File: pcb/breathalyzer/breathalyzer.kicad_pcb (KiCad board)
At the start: 2 copper layers, 18 parts, among them IC1 TPS3840DL25DBVR, J1 10129379-906002BLF, U1 STM32F030K6Tx, U2 TLV73325PDBV, U3 TLV61070ADBV

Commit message: reset button
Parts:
- added SW1: PTS636SK43SMTR, breathalyzer:PTS636SM43JSMTRLFS, F.Cu at (154.2, 119.4)
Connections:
- J1 pad 5: unconnected-(J1-Pad5) -> SWCLK
- J1 pad 6: unconnected-(J1-Pad6) -> SWDIO
- U1 pad 23: unconnected-(U1-PA13-Pad23) -> SWDIO
- U1 pad 24: unconnected-(U1-PA14-Pad24) -> SWCLK
- U1 pad 4: unconnected-(U1-NRST-Pad4) -> NRST

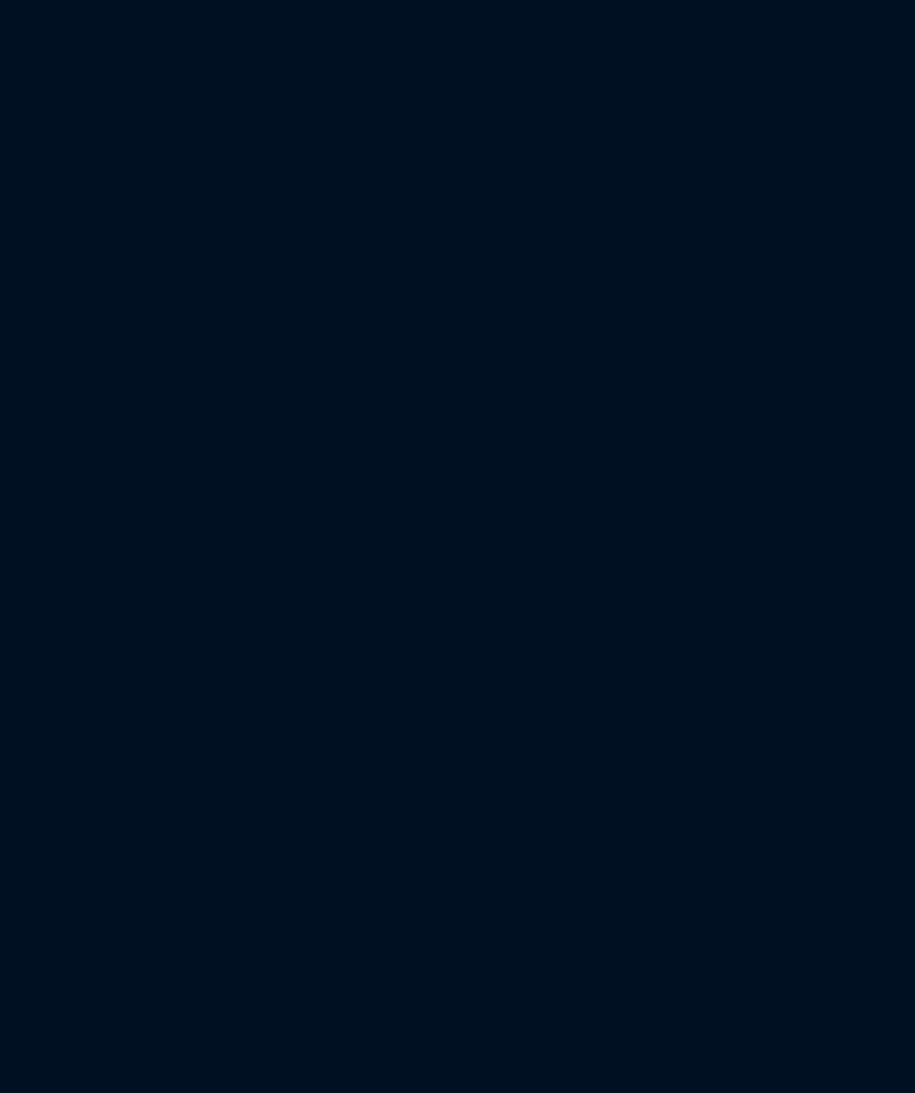
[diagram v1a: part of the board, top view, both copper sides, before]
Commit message: display parts chosen
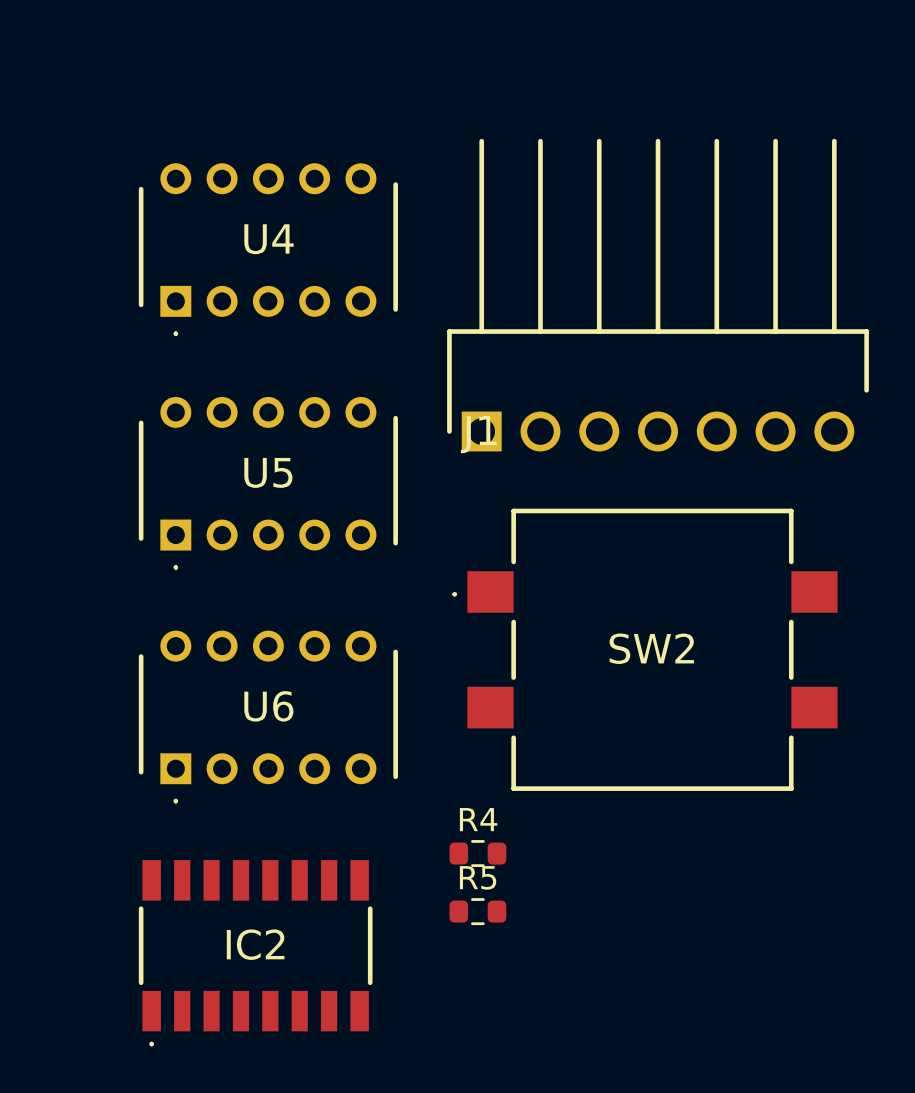
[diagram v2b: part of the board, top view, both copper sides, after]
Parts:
- added IC2: HEF4543BT,653, breathalyzer:HEF4543BT653, F.Cu at (181.6, 129.7)
- added J1: Conn_01x07_Pin, breathalyzer:HDRRA7W66P0X254_1X7_1778X229X274P, F.Cu at (191.4, 107.4)
- added R4: 10k, Resistor_SMD:R_0603_1608Metric, F.Cu at (191.2, 125.7)
- added R5: 10k, Resistor_SMD:R_0603_1608Metric, F.Cu at (191.2, 128.2)
- added SW2: 430162085826, breathalyzer:430162085826, F.Cu at (198.7, 116.9)
- added U4: HDSP-211C, breathalyzer:LDSA3502RDSUG, F.Cu at (178.1, 101.8)
- added U5: HDSP-211C, breathalyzer:LDSA3502RDSUG, F.Cu at (178.1, 111.9)
- added U6: HDSP-211C, breathalyzer:LDSA3502RDSUG, F.Cu at (178.1, 122.0)
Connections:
- U1 pad 6: unconnected-(U1-PA0-Pad6) -> WKUP

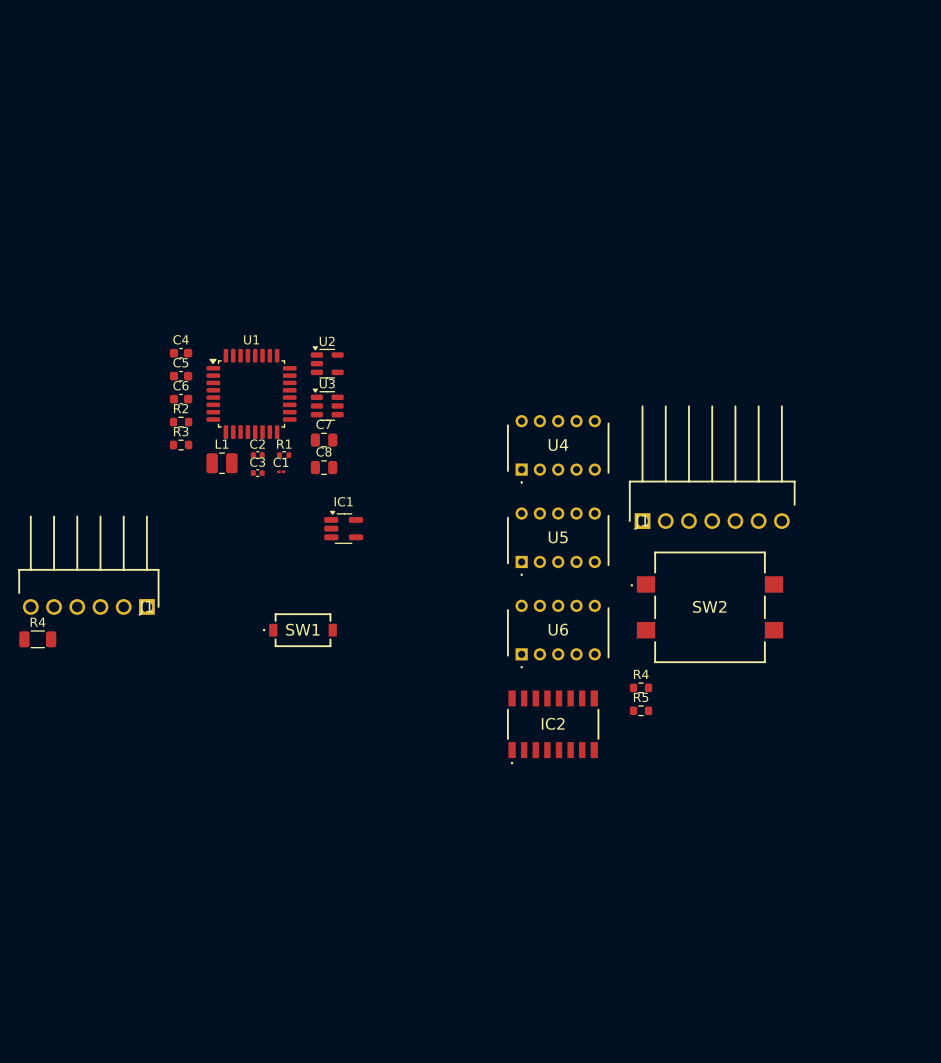
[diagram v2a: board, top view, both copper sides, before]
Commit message: numeric LCD display and driver
+5V boost
previous parts scrapped
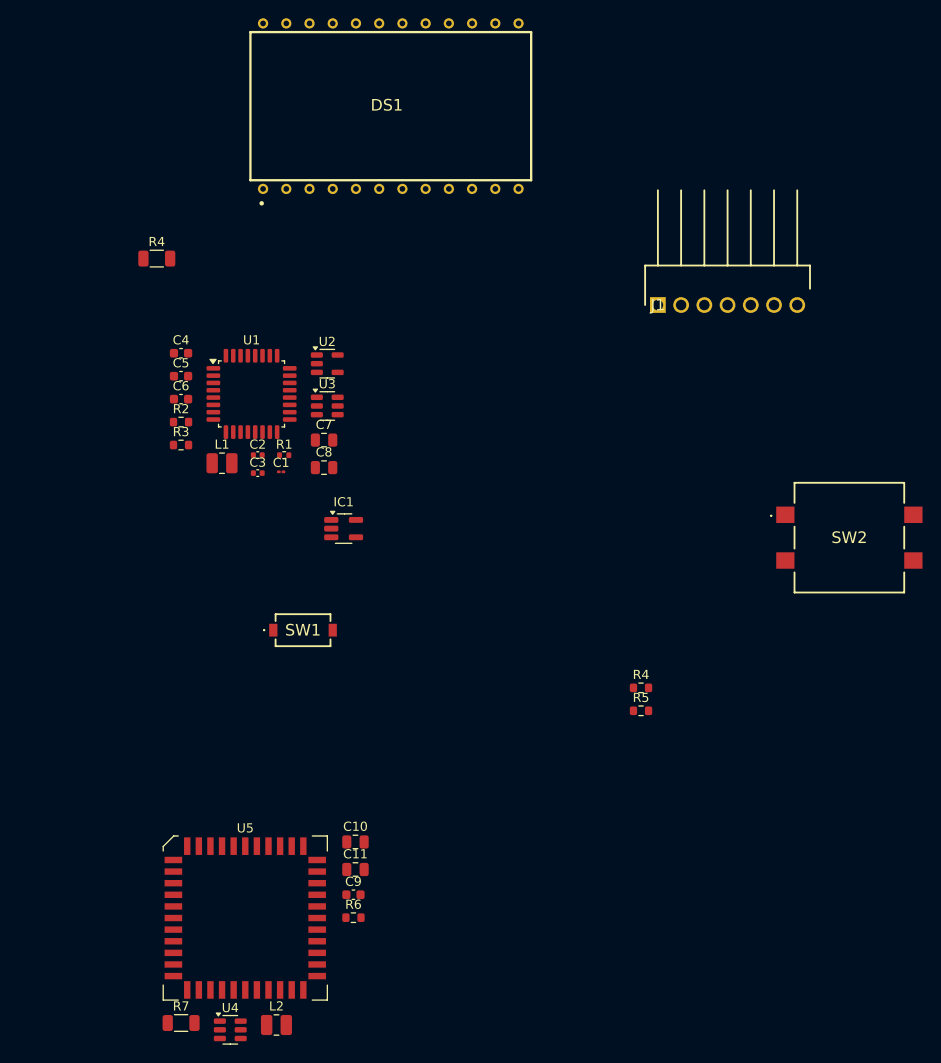
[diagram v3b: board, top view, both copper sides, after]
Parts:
- removed IC2: HEF4543BT,653, breathalyzer:HEF4543BT653
- removed the J1 at (137.2, 116.8)
- removed U6: HDSP-211C, breathalyzer:LDSA3502RDSUG
- added C10: 10 uF, Capacitor_SMD:C_0805_2012Metric, F.Cu at (160.0, 142.5)
- added C11: 10 uF, Capacitor_SMD:C_0805_2012Metric, F.Cu at (160.0, 145.6)
- added C9: 39 pF, Capacitor_SMD:C_0603_1608Metric, F.Cu at (159.7, 148.3)
- added DS1: LCD-S301C31TR, breathalyzer:LCD-S301C31TR, F.Cu at (163.8, 62.1)
- added L2: 24 nH, Inductor_SMD:L_1008_2520Metric, F.Cu at (151.3, 162.6)
- added R6: 10k, Resistor_SMD:R_0603_1608Metric, F.Cu at (159.7, 150.8)
- added R7: 90k, Resistor_SMD:R_1206_3216Metric, F.Cu at (140.9, 162.3)
- U4: value HDSP-211C -> TLV61070ADBV; footprint breathalyzer:LDSA3502RDSUG -> Package_TO_SOT_SMD:SOT-23-6
- U5: value HDSP-211C -> AY0438X-L; footprint breathalyzer:LDSA3502RDSUG -> Package_LCC:PLCC-44
- moved U4 69.1 mm to (146.3, 163.1)
- moved U5 49.3 mm to (147.9, 150.9)
- moved R4 43.6 mm to (138.2, 78.7)
- moved J1 23.7 mm to (193.0, 83.8)
- moved SW2 17.0 mm to (214.0, 109.3)
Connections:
- U1 pad 12: unconnected-(U1-PA6-Pad12) -> LCD_Clock
- U1 pad 8: unconnected-(U1-PA2-Pad8) -> LCD_DATA
- U1 pad 9: unconnected-(U1-PA3-Pad9) -> LCD_LOAD
- U4 pad 1: unconnected-(U4-CA-Pad1) -> Net-(U4-SW)
- U4 pad 2: unconnected-(U4-F-Pad2) -> GND
- U4 pad 3: unconnected-(U4-G-Pad3) -> Net-(IC1-~{RESET})
- U4 pad 4: unconnected-(U4-E-Pad4) -> Net-(U4-V_{FB})
- U4 pad 5: unconnected-(U4-D-Pad5) -> +5V
- U4 pad 6: unconnected-(U4-CA-Pad6) -> +BATT
- U5 pad 1: unconnected-(U5-CA-Pad1) -> +5V
- U5 pad 2: unconnected-(U5-F-Pad2) -> LCD_LOAD

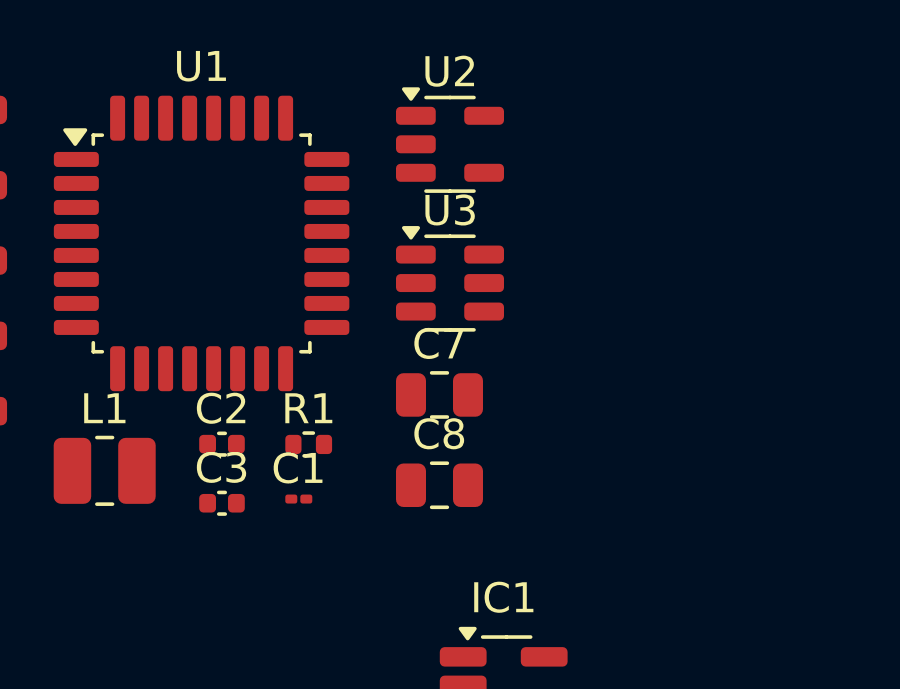
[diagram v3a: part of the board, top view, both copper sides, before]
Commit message: removed 3V3 boost
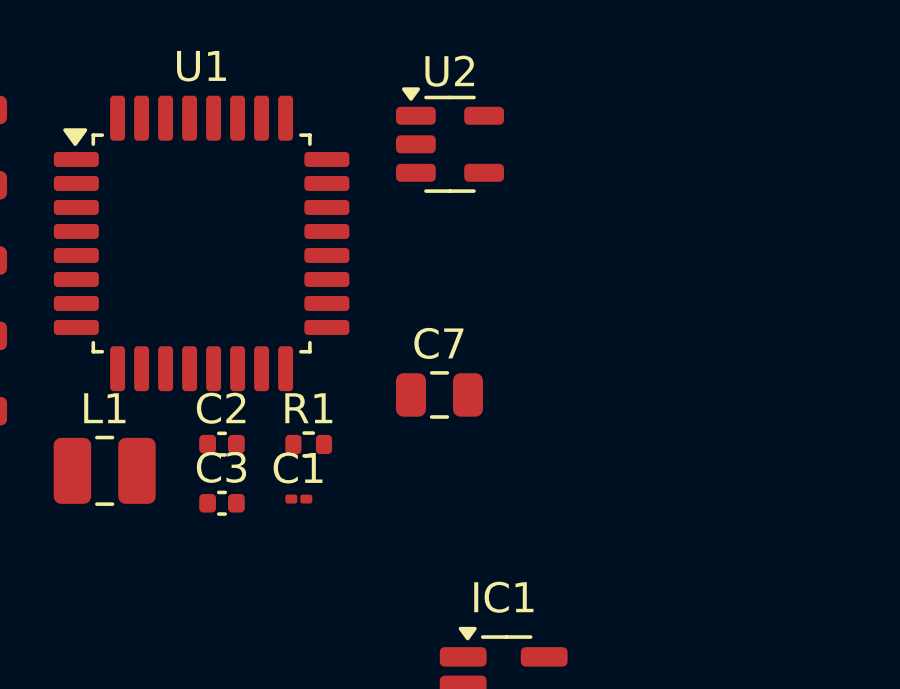
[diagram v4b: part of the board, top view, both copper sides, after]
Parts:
- removed C8: 10 uF, Capacitor_SMD:C_0805_2012Metric
- removed U3: TLV61070ADBV, Package_TO_SOT_SMD:SOT-23-6
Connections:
- C1 pad 1: +3V3 -> +2V5
- C2 pad 1: +3V3 -> +2V5
- C3 pad 1: +3V3 -> +2V5
- J1 pad 3: +3V3 -> +2V5
- SW2 pad 2: +3V3 -> +2V5
- U1 pad 1: +3V3 -> +2V5
- U1 pad 10: unconnected-(U1-PA4-Pad10) -> 5V_EN
- U1 pad 17: +3V3 -> +2V5
- U1 pad 5: +3V3 -> +2V5
- U4 pad 3: Net-(IC1-~{RESET}) -> 5V_EN

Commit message: buzzer
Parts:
- added BZ1: Buzzer, breathalyzer:CPT1414680T, F.Cu at (182.9, 144.8)
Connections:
- R5 pad 1: WKUP -> USERBUTTON
- SW2 pad 1: WKUP -> USERBUTTON
- U1 pad 15: unconnected-(U1-PB1-Pad15) -> USERBUTTON
- U1 pad 18: unconnected-(U1-PA8-Pad18) -> BUZZER
- U1 pad 6: WKUP -> USERBUTTON

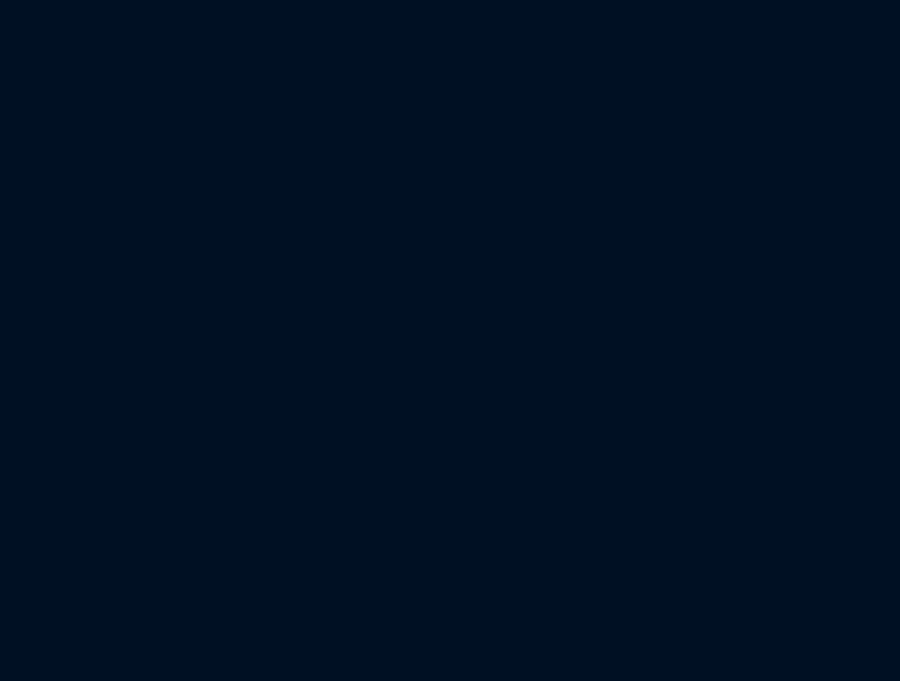
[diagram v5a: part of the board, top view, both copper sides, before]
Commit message: reverse polarity protection
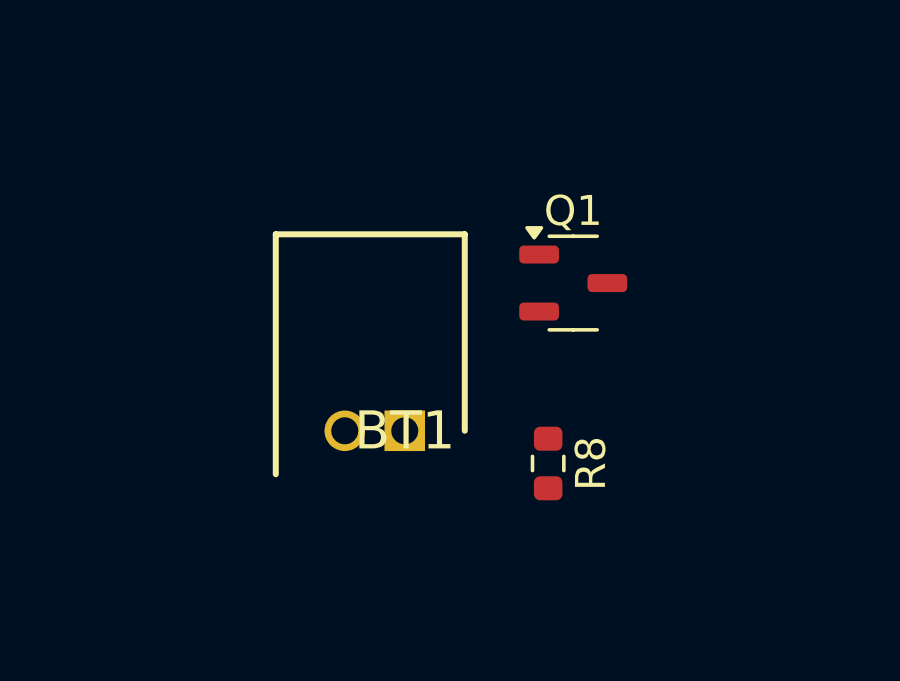
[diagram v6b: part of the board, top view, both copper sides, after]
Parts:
- added BT1: Battery, breathalyzer:SHDRRA2W50P0X200_1X2_600X770X525P, F.Cu at (206.6, 133.5)
- added Q1: Q_PMOS, Package_TO_SOT_SMD:SOT-23-3, F.Cu at (212.2, 128.6)
- added R8: 1k, Resistor_SMD:R_0603_1608Metric, F.Cu at (211.4, 134.6)

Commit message: changed power supply
5V boost from BATT
2V5 LDO from 5V
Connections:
- C4 pad 2: +BATT -> +5V
- SW2 pad 2: +2V5 -> (no net)
- SW2 pad 3: (no net) -> +2V5
- U1 pad 10: 5V_EN -> unconnected-(U1-PA4-Pad10)
- U2 pad 1: +BATT -> +5V
- U2 pad 3: Net-(IC1-~{RESET}) -> +5V
- U4 pad 3: 5V_EN -> +BATT
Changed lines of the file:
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@@
 	(net 16 "SWCLK")
 	(net 17 "unconnected-(U1-PB7-Pad30)")
-	(net 18 "5V_EN")
+	(net 18 "unconnected-(U1-PA4-Pad10)")
 	(net 19 "Net-(U5-LCD0)")
 	(net 20 "Net-(U4-V_{FB})")
@@
 			(layers "F.Cu" "F.Mask" "F.Paste")
 			(roundrect_rratio 0.25)
-			(net 2 "+BATT")
+			(net 21 "+5V")
 			(pintype "passive")
 		)
@@
 			(layers "F.Cu" "F.Mask" "F.Paste")
 			(roundrect_rratio 0.25)
-			(net 18 "5V_EN")
+			(net 2 "+BATT")
 			(pinfunction "EN")
 			(pintype "input")
@@
 			(layers "F.Cu" "F.Mask" "F.Paste")
 			(roundrect_rratio 0.25)
-			(net 2 "+BATT")
+			(net 21 "+5V")
 			(pinfunction "IN")
 			(pintype "power_in")
@@
 			(layers "F.Cu" "F.Mask" "F.Paste")
 			(roundrect_rratio 0.25)
-			(net 6 "Net-(IC1-~{RESET})")
+			(net 21 "+5V")
 			(pinfunction "EN")
 			(pintype "input")
@@
 			(layers "F.Cu" "F.Mask" "F.Paste")
 			(roundrect_rratio 0.25)
-			(net 18 "5V_EN")
+			(net 18 "unconnected-(U1-PA4-Pad10)")
 			(pinfunction "PA4")
 			(pintype "bidirectional")
@@
 			(size 1.8 2)
 			(layers "F.Cu" "F.Mask" "F.Paste")
-			(net 3 "+2V5")
-			(pinfunction "2")
-			(pintype "passive")
 		)
 		(pad "3" smd rect
@@
 			(size 1.8 2)
 			(layers "F.Cu" "F.Mask" "F.Paste")
+			(net 3 "+2V5")
+			(pinfunction "3")
+			(pintype "passive")
 		)
 		(pad "4" smd rect

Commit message: sensor connector
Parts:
- added J2: MP-3B socket, breathalyzer:25SHB04TS, F.Cu at (188.0, 114.3)
- added Q2: NPN, Package_TO_SOT_SMD:SOT-23-3, F.Cu at (128.4, 127.0)
- added R1: 50k_Variable, Potentiometer_THT:Potentiometer_ACP_CA9-H5_Horizontal, F.Cu at (127.1, 108.4)
- added R2: 330, Resistor_SMD:R_0805_2012Metric, F.Cu at (136.2, 106.7)
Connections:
- U1 pad 10: unconnected-(U1-PA4-Pad10) -> SENSOR_EN
- U1 pad 7: unconnected-(U1-PA1-Pad7) -> ADC_IN
